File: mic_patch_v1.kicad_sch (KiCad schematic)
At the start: 0 parts

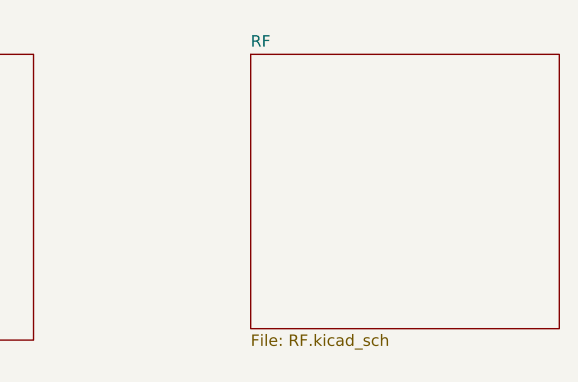
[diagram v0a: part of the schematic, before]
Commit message: updated power supply to 3.0V to support micro SD card
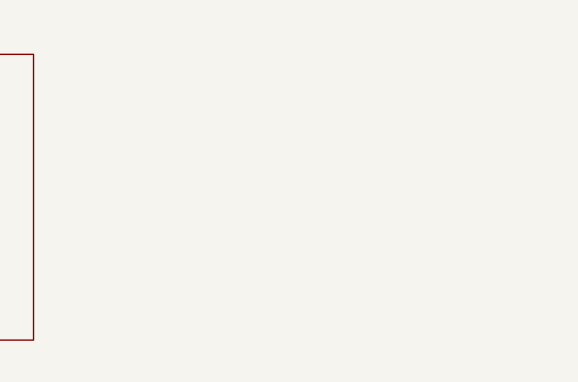
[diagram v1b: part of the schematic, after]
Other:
- removed sheet RF
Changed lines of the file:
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@@
-		)
-	)
-	(sheet
-		(at 208.28 59.69)
-		(size 34.29 30.48)
-		(fields_autoplaced yes)
-		(stroke
-			(width 0.1524)
-			(type solid)
-		)
-		(fill
-			(color 0 0 0 0.0000)
-		)
-		(property "Sheetname" "RF"
-			(at 208.28 58.9784 0)
-			(effects
-				(font
-					(size 1.27 1.27)
-				)
-				(justify left bottom)
-			)
-		)
-		(property "Sheetfile" "RF.kicad_sch"
-			(at 208.28 90.7546 0)
-			(effects
-				(font
-					(size 1.27 1.27)
-				)
-				(justify left top)
-			)
-		)
-		(instances
-			(project "mic_patch_v1"
-				(path "/5448a297-4261-40a5-8009-47199bfe22cb"
-					(page "5")
-				)
-			)
 		)
 	)

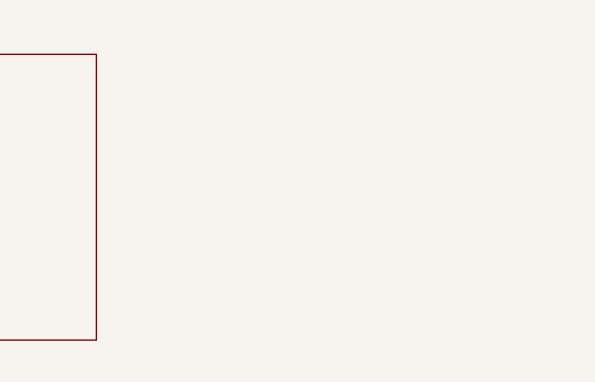
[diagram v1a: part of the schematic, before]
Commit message: routed pins for SD card
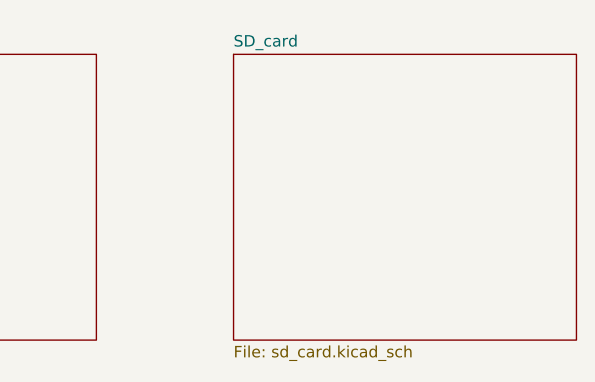
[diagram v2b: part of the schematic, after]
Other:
- added sheet SD_card (sd_card.kicad_sch)
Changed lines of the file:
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@@
+		)
+	)
+	(sheet
+		(at 199.39 59.69)
+		(size 38.1 31.75)
+		(fields_autoplaced yes)
+		(stroke
+			(width 0.1524)
+			(type solid)
+		)
+		(fill
+			(color 0 0 0 0.0000)
+		)
+		(property "Sheetname" "SD_card"
+			(at 199.39 58.9784 0)
+			(effects
+				(font
+					(size 1.27 1.27)
+				)
+				(justify left bottom)
+			)
+		)
+		(property "Sheetfile" "sd_card.kicad_sch"
+			(at 199.39 92.0246 0)
+			(effects
+				(font
+					(size 1.27 1.27)
+				)
+				(justify left top)
+			)
+		)
+		(instances
+			(project "mic_patch_v1"
+				(path "/5448a297-4261-40a5-8009-47199bfe22cb"
+					(page "5")
+				)
+			)
 		)
 	)

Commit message: Removed SD Card from schematic
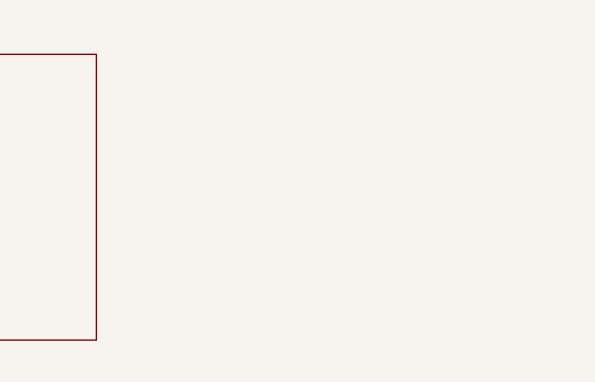
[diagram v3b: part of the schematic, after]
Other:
- removed sheet SD_card
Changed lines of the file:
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@@
-		)
-	)
-	(sheet
-		(at 199.39 59.69)
-		(size 38.1 31.75)
-		(fields_autoplaced yes)
-		(stroke
-			(width 0.1524)
-			(type solid)
-		)
-		(fill
-			(color 0 0 0 0.0000)
-		)
-		(property "Sheetname" "SD_card"
-			(at 199.39 58.9784 0)
-			(effects
-				(font
-					(size 1.27 1.27)
-				)
-				(justify left bottom)
-			)
-		)
-		(property "Sheetfile" "sd_card.kicad_sch"
-			(at 199.39 92.0246 0)
-			(effects
-				(font
-					(size 1.27 1.27)
-				)
-				(justify left top)
-			)
-		)
-		(instances
-			(project "mic_patch_v1"
-				(path "/5448a297-4261-40a5-8009-47199bfe22cb"
-					(page "5")
-				)
-			)
 		)
 	)
